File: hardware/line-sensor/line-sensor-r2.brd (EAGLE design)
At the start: 106 x 54 mm, 72 parts, among them IC1 GP2S60, IC10 GP2S60, IC11 GP2S60, IC12 GP2S60, IC13 GP2S60, IC14 GP2S60, IC15 GP2S60, IC16 GP2S60, IC17 GP2S60, IC18 GP2S60, IC19 GP2S60, IC2 GP2S60, IC20 GP2S60, IC21 GP2S60, IC22 GP2S60, IC23 GP2S60, IC3 GP2S60, IC4 GP2S60, IC5 GP2S60, IC6 GP2S60, IC7 GP2S60, IC8 GP2S60, IC9 GP2S60

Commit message: - fixed some DRC errors
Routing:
- net AGND: track 195.2 -> 187.7 mm
- net SENSOR_19: track 58.1 -> 59.2 mm
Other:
- board text added: "1"
- board text added: "S1"
- board text added: "S23"
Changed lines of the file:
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@@
 </layers>
 <board>
-<fusionsync huburn="a.cGVyc29uYWw6dWUyOTRhMzFm" projecturn="a.cGVyc29uYWw6dWUyOTRhMzFmIzIwMTUwOTAxMTYzMzEyNTY" f3durn="urn:adsk.wipprod:dm.lineage:2VtSV_9sQRCPOwD1aunNyg" pcbguid="1db26d2e-9563-459f-8ff3-fe5aac38d394" lastpulledtime="" lastsyncedchangeguid="954131dc-718e-a5c1-85f6-09fde677fd1e"/>
+<fusionsync huburn="a.cGVyc29uYWw6dWUyOTRhMzFm" projecturn="a.cGVyc29uYWw6dWUyOTRhMzFmIzIwMTUwOTAxMTYzMzEyNTY" f3durn="urn:adsk.wipprod:dm.lineage:2VtSV_9sQRCPOwD1aunNyg" pcbguid="1db26d2e-9563-459f-8ff3-fe5aac38d394" lastpulledtime="" lastsyncedchangeguid="e6f0f685-80a9-5ac7-ca9b-22654323d5f4"/>
 <plain>
 <wire x1="27" y1="52" x2="66" y2="52" width="0" layer="20"/>
@@
 <wire x1="77" y1="70.5" x2="77" y2="67" width="0.3" layer="25"/>
 <wire x1="126" y1="67" x2="132.5" y2="67" width="0.3" layer="25"/>
-<wire x1="126" y1="61" x2="132.5" y2="61" width="0.3" layer="25"/>
+<wire x1="127" y1="61" x2="132.5" y2="61" width="0.3" layer="25"/>
+<text x="36" y="60" size="1.778" layer="25" align="center">S1</text>
+<text x="124" y="60" size="1.778" layer="25" align="center">S23</text>
+<text x="70" y="29" size="1.778" layer="26" rot="MR0">1</text>
 </plain>
 <attributes>
@@
 </class>
 </classes>
-<designrules name="oshpark-2layer">
+<designrules name="oshpark-2layer *">
 <description language="en">&lt;b&gt;OSH Park Design Rules&lt;/b&gt;
 &lt;p&gt;
@@
 <element name="IC8" library="sensors" library_urn="urn:adsk.eagle:library:699948" package="GP2S60" package3d_urn="urn:adsk.eagle:package:699951/9" value="GP2S60" x="64" y="64" rot="R111.8"/>
 <element name="IC9" library="sensors" library_urn="urn:adsk.eagle:library:699948" package="GP2S60" package3d_urn="urn:adsk.eagle:package:699951/9" value="GP2S60" x="68" y="64" rot="R111.8"/>
-<element name="JP1" library="connectors" library_urn="urn:adsk.eagle:library:5574234" package="MOLEX-501931-3070" package3d_urn="urn:adsk.eagle:package:6453715/2" value="MOLEX-501931-3070" x="80" y="23" rot="MR0">
-<attribute name="NAME" x="80" y="18.6" size="1.27" layer="26" rot="MR0" align="center"/>
-</element>
+<element name="JP1" library="connectors" library_urn="urn:adsk.eagle:library:5574234" package="MOLEX-501931-3070" package3d_urn="urn:adsk.eagle:package:6453715/2" value="MOLEX-501931-3070" x="80" y="23" rot="MR0"/>
 <element name="R1" library="resistors" library_urn="urn:adsk.eagle:library:704770" package="RESISTOR-0603" package3d_urn="urn:adsk.eagle:package:704947/3" value="1k" x="36" y="66" rot="MR180"/>
 <element name="R10" library="resistors" library_urn="urn:adsk.eagle:library:704770" package="RESISTOR-0603" package3d_urn="urn:adsk.eagle:package:704947/3" value="220k" x="52" y="63" rot="MR180"/>
@@
 <wire x1="70" y1="18" x2="69.425" y2="18.575" width="0.3" layer="16"/>
 <wire x1="69.425" y1="18.575" x2="69.425" y2="19.875" width="0.3" layer="16"/>
-<wire x1="69.425" y1="19.875" x2="69" y2="20.3" width="0.3" layer="16"/>
-<wire x1="69" y1="20.3" x2="69" y2="27" width="0.3" layer="16"/>
-<wire x1="70" y1="23" x2="70" y2="27" width="0.3" layer="16"/>
 <wire x1="71.25" y1="21.75" x2="70" y2="23" width="0.3" layer="16"/>
-<wire x1="69.425" y1="27.075" x2="69" y2="27.5" width="0.3" layer="16"/>
 <wire x1="88.75" y1="25.9" x2="89.925" y2="27.075" width="0.3" layer="16"/>
 <wire x1="89.925" y1="27.075" x2="90.575" y2="27.075" width="0.3" layer="16"/>
@@
 <wire x1="64" y1="56.25" x2="64" y2="55" width="0.3" layer="16"/>
 <wire x1="90.575" y1="27.075" x2="90.575" y2="33.425" width="0.6" layer="16"/>
-<wire x1="90.575" y1="33.425" x2="90.5" y2="33.5" width="0.6" layer="16"/>
 <wire x1="69.425" y1="27.075" x2="69.425" y2="28.575" width="0.6" layer="16"/>
 <wire x1="69.425" y1="28.575" x2="68" y2="30" width="0.6" layer="16"/>
-<wire x1="68" y1="30" x2="68" y2="37" width="0.6" layer="16"/>
-<wire x1="69.425" y1="27.075" x2="70" y2="27" width="0" layer="19" extent="16-16"/>
-<wire x1="69" y1="27" x2="69.425" y2="27.075" width="0" layer="19" extent="16-16"/>
+<wire x1="70" y1="23" x2="70" y2="26.5" width="0.3" layer="16"/>
+<wire x1="70" y1="26.5" x2="69.425" y2="27.075" width="0.3" layer="16"/>
+<wire x1="69.425" y1="19.875" x2="69.425" y2="27.075" width="0.3" layer="16"/>
 </signal>
 <signal name="SENSOR_1">
@@
 <wire x1="43" y1="63" x2="42" y2="62" width="0.3" layer="16"/>
 <via x="42" y="62" extent="1-16" drill="0.35"/>
-<wire x1="42" y1="62" x2="42.009265625" y2="62" width="0.3" layer="1"/>
 <wire x1="42" y1="62" x2="43" y2="61" width="0.3" layer="1"/>
 <wire x1="43" y1="61" x2="44.009265625" y2="61" width="0.3" layer="1"/>
@@
 <wire x1="51" y1="63" x2="50" y2="62" width="0.3" layer="16"/>
 <via x="50" y="62" extent="1-16" drill="0.35"/>
-<wire x1="50" y1="62" x2="50.01853125" y2="62" width="0.3" layer="1"/>
 <wire x1="50" y1="62" x2="51" y2="61" width="0.3" layer="1"/>
 <wire x1="51" y1="61" x2="52.009265625" y2="61" width="0.3" layer="1"/>
@@
 <contactref element="JP1" pad="12"/>
 <wire x1="68" y1="61" x2="76.8" y2="52.2" width="0.3" layer="1"/>
-<wire x1="64.009265625" y1="63.303640625" x2="64.009265625" y2="62.990734375" width="0.3" layer="1"/>
 <wire x1="63.25" y1="63" x2="63" y2="63" width="0.3" layer="16"/>
 <wire x1="63" y1="63" x2="62" y2="62" width="0.3" layer="16"/>
 <via x="62" y="62" extent="1-16" drill="0.35"/>
 <wire x1="68" y1="61" x2="65" y2="61" width="0.3" layer="1"/>
-<wire x1="62" y1="62" x2="62.009265625" y2="61.990734375" width="0.3" layer="1"/>
 <wire x1="62" y1="62" x2="63" y2="61" width="0.3" layer="1"/>
 <wire x1="63" y1="61" x2="64" y2="61" width="0.3" layer="1"/>
@@
 <wire x1="80.009265625" y1="63.303640625" x2="80.009265625" y2="61" width="0.3" layer="1"/>
 <wire x1="80.009265625" y1="61" x2="80.009265625" y2="34.009265625" width="0.3" layer="1"/>
-<wire x1="80.009265625" y1="34.009265625" x2="80" y2="34" width="0.3" layer="1"/>
 <wire x1="79.25" y1="63" x2="79" y2="63" width="0.3" layer="16"/>
 <wire x1="79" y1="63" x2="78" y2="62" width="0.3" layer="16"/>
@@
 <wire x1="83" y1="61" x2="84.009265625" y2="61" width="0.3" layer="1"/>
 <via x="80.8" y="29" extent="1-16" drill="0.35"/>
-<wire x1="81" y1="26.15" x2="81.25" y2="25.9" width="0.3" layer="16"/>
 <wire x1="80.8" y1="52.8" x2="80.8" y2="29" width="0.3" layer="1"/>
 <wire x1="81.25" y1="25.9" x2="81.25" y2="27.75" width="0.3" layer="16"/>
@@
 <wire x1="85.6" y1="51.6" x2="85.6" y2="29" width="0.3" layer="1"/>
 <wire x1="85.6" y1="29" x2="85" y2="28.4" width="0.3" layer="16"/>
-<wire x1="85" y1="28.4" x2="85" y2="27" width="0.3" layer="16"/>
-<wire x1="85" y1="27" x2="85" y2="25.9" width="0" layer="19" extent="16-16"/>
+<wire x1="85" y1="28.4" x2="85" y2="28.4" width="0.3" layer="16"/>
+<wire x1="85" y1="28.4" x2="85" y2="28.4" width="0.3" layer="16"/>
+<wire x1="85" y1="28.4" x2="85" y2="25.9" width="0.3" layer="16"/>
 </signal>
 <signal name="SENSOR_20">
@@
 <mfgpreviewcolor name="substratecolor" color="0xFF786E46"/>
 </mfgpreviewcolors>
+<errors>
+</errors>
 </board>
 </drawing>

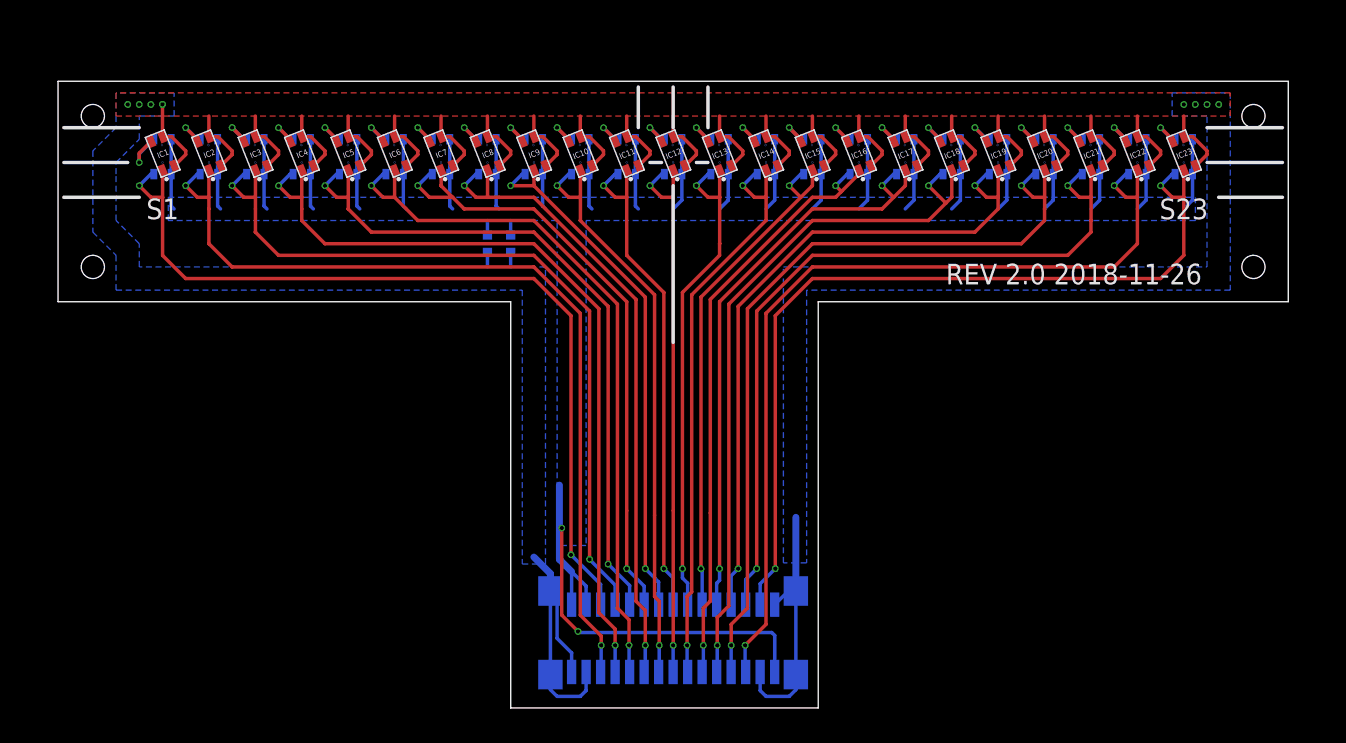
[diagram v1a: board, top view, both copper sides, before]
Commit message: - added voltage sources for line sensor (not complete)
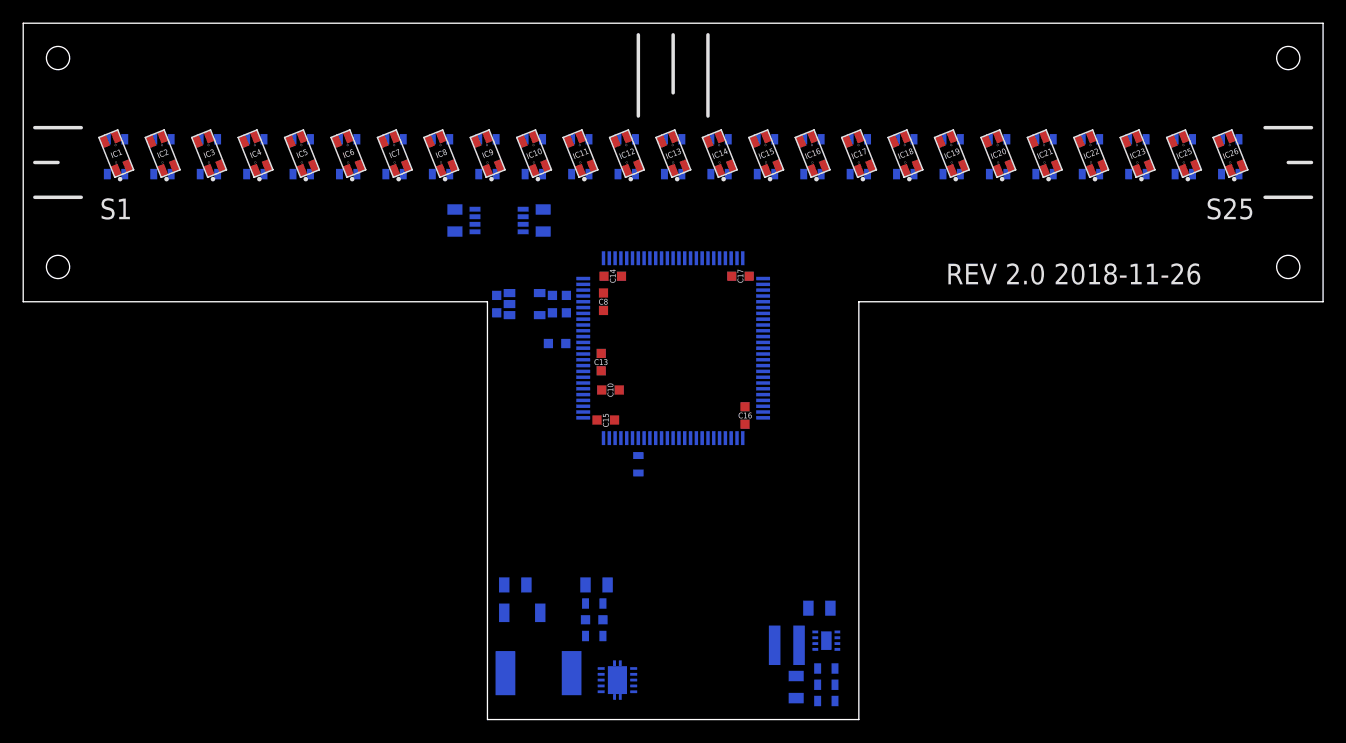
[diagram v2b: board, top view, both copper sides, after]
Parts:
- removed JP1: MOLEX-501931-3070, connectors:MOLEX-501931-3070
- added C10, C13, C14, C15, C16, C17, C18: 0.1u, capacitors:CAPACITOR-0603
- added C11: 33n 10V X7R, capacitors:CAPACITOR-0603
- added C12: 4.7u, capacitors:CAPACITOR-0805
- added C19: 22u 10V X7R, capacitors:CAPACITOR-0805
- added C3, C4: 1u 10V X7R, capacitors:CAPACITOR-0805
- added C5: 1u, capacitors:CAPACITOR-0603
- added C6: 1u 50V X7R, capacitors:CAPACITOR-1206
- added C7: 22u 10V X7S, capacitors:CAPACITOR-0805
- added C8: 0.1u 10V X7R, capacitors:CAPACITOR-0603
- added C9: 10u 50V X7R, capacitors:CAPACITOR-0805
- added IC24: STM32L151VE, mcu:LQFP100_14X14
- added IC25, IC26: GP2S60, sensors:GP2S60
- added IC27: ADR366BUJZ, voltage-source:TSOT-25
- added IC28: TI-TPS62170, voltage-source:WSON-8-0.5MM
- added IC29: TI-LM5165YDRCR, voltage-source:VSON-10-0.5MM
- added IC30: ADP124ARHZ-3.3-R7CT-ND, voltage-source:MSOP-8
- added L1: 3.3u 2.63A, inductors:VLS3012HBX
- added L2: 150u 0.35A, inductors:ELL-6SH151M
- added R47, R49: 1k, resistors:RESISTOR-0603
- added R48, R50: 220k, resistors:RESISTOR-0603
- added R51: 121k 1%, resistors:RESISTOR-0603
- added R52: 100k 1%, resistors:RESISTOR-0603
- added R53: 0.5 1%, resistors:RESISTOR-0603
- added R54: 100k, resistors:RESISTOR-0603
- added R55: 610k 1%, resistors:RESISTOR-0603
- added R56: 180k 1%, resistors:RESISTOR-0603
- C1: value 0.1u -> 0.1u 10V
- C2: value 10u -> 0.1u 50V
- moved C1 7.08 mm to (70.8, 51.8)
- moved C2 5.26 mm to (64.8, 51.8)
- moved IC1 4.00 mm to (32.0, 64.0)
- moved IC10 4.00 mm to (68.0, 64.0)
- moved IC11 4.00 mm to (72.0, 64.0)
- moved IC12 4.00 mm to (76.0, 64.0)
- moved IC13 4.00 mm to (80.0, 64.0)
- moved IC14 4.00 mm to (84.0, 64.0)
- moved IC15 4.00 mm to (88.0, 64.0)
- moved IC16 4.00 mm to (92.0, 64.0)
- moved IC17 4.00 mm to (96.0, 64.0)
- moved IC18 4.00 mm to (100.0, 64.0)
- moved IC19 4.00 mm to (104.0, 64.0)
- moved IC2 4.00 mm to (36.0, 64.0)
- moved IC20 4.00 mm to (108.0, 64.0)
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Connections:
- new net !RST: C18.1, IC24.14
- new net 3V1: R47.P$2, R48.P$2
- new net 3V2: R49.P$2, R50.P$2
- new net BOOT0: IC24.94, R54.P$1
- new net DGND: C10.2, C11.2, C12.2, C13.2, C14.2, C15.2, C16.2, C17.2, C18.2, C7.2, IC24.10, IC24.27, IC24.49, IC24.74, IC24.99, IC29.10, IC29.11, IC29.3, R54.P$2
- new net GND: C19.2, C2.2, C4.2, C6.P$2, C9.2, IC27.2, IC28.1, IC28.4, IC28.9, R51.P$2, R56.P$1
- new net N$24: IC25.4, R47.P$1
- new net N$25: IC26.4, R49.P$1
- new net N$26: IC28.7, L1.1
- new net N$27: IC28.8, R52.P$1
- new net N$28: C11.1, IC29.4
- new net N$29: IC29.1, L2.1
- new net N$30: IC29.5, R51.P$1
- new net N$31: IC28.5, R55.P$1, R56.P$2
- new net N$32: C7.1, R53.P$2
- new net SENSOR_24: IC24.53, IC25.1, R48.P$1
- new net SENSOR_25: IC24.54, IC26.1, R50.P$1
- new net V3.5: C19.1, C4.1, IC28.6, IC30.5, IC30.7, IC30.8, L1.2, R52.P$2, R55.P$2
- new net VBAT: C2.1, C6.P$1, C9.1, IC27.3, IC28.2, IC28.3, IC29.2, IC29.7
- new net VDD: C10.1, C12.1, C13.1, C14.1, C15.1, C16.1, C17.1, IC24.100, IC24.11, IC24.28, IC24.50, IC24.6, IC24.75, IC29.8, L2.2, R53.P$1
- new net VDDA: C3.1, C8.1, IC24.22, IC30.1, IC30.2, IC30.3
- new net VREF3.3: C1.1, C5.1, IC24.21, IC27.4
- net 3V3: no longer C1.1, C2.1, JP1.1, JP1.3, JP1.30
- net AGND: now also C3.2, C5.2, C8.2, IC24.19, IC24.20, IC25.2, IC25.3, IC26.2, IC26.3, IC30.4; no longer C2.2, JP1.2, JP1.28, JP1.29, JP1.4, JP1.NAIL1, JP1.NAIL2, JP1.NAIL3, JP1.NAIL4
- net SENSOR_1: now also IC24.15; no longer JP1.5
- net SENSOR_10: now also IC24.30; no longer JP1.14
- net SENSOR_11: now also IC24.31; no longer JP1.15
- net SENSOR_12: now also IC24.32; no longer JP1.16
- net SENSOR_13: now also IC24.33; no longer JP1.17
- net SENSOR_14: now also IC24.34; no longer JP1.18
- net SENSOR_15: now also IC24.35; no longer JP1.19
- net SENSOR_16: now also IC24.36; no longer JP1.20
- net SENSOR_17: now also IC24.37; no longer JP1.21
- net SENSOR_18: now also IC24.38; no longer JP1.22
- net SENSOR_19: now also IC24.39; no longer JP1.23
- net SENSOR_2: now also IC24.16; no longer JP1.6
- net SENSOR_20: now also IC24.40; no longer JP1.24
- net SENSOR_21: now also IC24.41; no longer JP1.25
- net SENSOR_22: now also IC24.51; no longer JP1.26
- net SENSOR_23: now also IC24.52; no longer JP1.27
- net SENSOR_3: now also IC24.17; no longer JP1.7
- net SENSOR_4: now also IC24.18; no longer JP1.8
- net SENSOR_5: now also IC24.23; no longer JP1.9
- net SENSOR_6: now also IC24.24; no longer JP1.10
- net SENSOR_7: now also IC24.25; no longer JP1.11
- net SENSOR_8: now also IC24.26; no longer JP1.12
- net SENSOR_9: now also IC24.29; no longer JP1.13
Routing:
- net 3V3: track 189.2 -> 0.00 mm, vias 2 -> 0
- net AGND: track 187.7 -> 0.00 mm, vias 8 -> 0
- net SENSOR_22: track 76.5 -> 0.00 mm, vias 2 -> 0
- net SENSOR_2: track 76.5 -> 0.00 mm, vias 2 -> 0
- net SENSOR_1: track 74.7 -> 0.00 mm, vias 2 -> 0
- net SENSOR_23: track 74.2 -> 0.00 mm, vias 2 -> 0
- net SENSOR_20: track 69.0 -> 0.00 mm, vias 2 -> 0
- net SENSOR_4: track 69.0 -> 0.00 mm, vias 2 -> 0
- net SENSOR_3: track 67.2 -> 0.00 mm, vias 2 -> 0
- net SENSOR_21: track 66.7 -> 0.00 mm, vias 2 -> 0
- net SENSOR_6: track 61.5 -> 0.00 mm, vias 2 -> 0
- net SENSOR_18: track 61.2 -> 0.00 mm, vias 2 -> 0
- net SENSOR_5: track 59.7 -> 0.00 mm, vias 2 -> 0
- net SENSOR_19: track 59.2 -> 0.00 mm, vias 2 -> 0
- net SENSOR_8: track 55.3 -> 0.00 mm, vias 2 -> 0
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- removed copper zone on layer 16, net 3V3
- removed copper zone on layer 1, net AGND
- removed copper zone on layer 16, net AGND
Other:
- board size 106 x 54 mm -> 112 x 60 mm
- board text added: "S25"
- board text removed: "1"
- board text removed: "S23"
